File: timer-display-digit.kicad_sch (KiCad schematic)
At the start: 6 parts, among them U1 SN74LS08, U2 SN74HC595DT, U3 SN74LS08

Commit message: production ready
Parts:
- U1, U3: DigiKey# (none) -> 296-14879-1-ND
- U2: DigiKey# (none) -> 296-31823-1-ND
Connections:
- net +5V: no longer U1.14 (VCC), U3.14 (VCC)
- net A: now also U1.3; no longer U1.8
- net Araw: now also U1.1; no longer U1.9
- net B: now also U1.3; no longer U1.11
- net Braw: now also U1.1; no longer U1.12
- net C: now also U3.3; no longer U3.8
- net Craw: now also U3.1; no longer U3.9
- net E: now also U3.3; no longer U3.6
- net Eraw: now also U3.1; no longer U3.4
- net F: now also U1.3; no longer U1.6
- net Fraw: now also U1.1; no longer U1.4
- net GND: now also U3.1, U3.2; no longer U1.7 (GND), U3.12, U3.13, U3.7 (GND)
- net PWM: now also U1.2, U1.2, U1.2, U3.2, U3.2; no longer U1.10, U1.13, U1.5, U3.10, U3.5

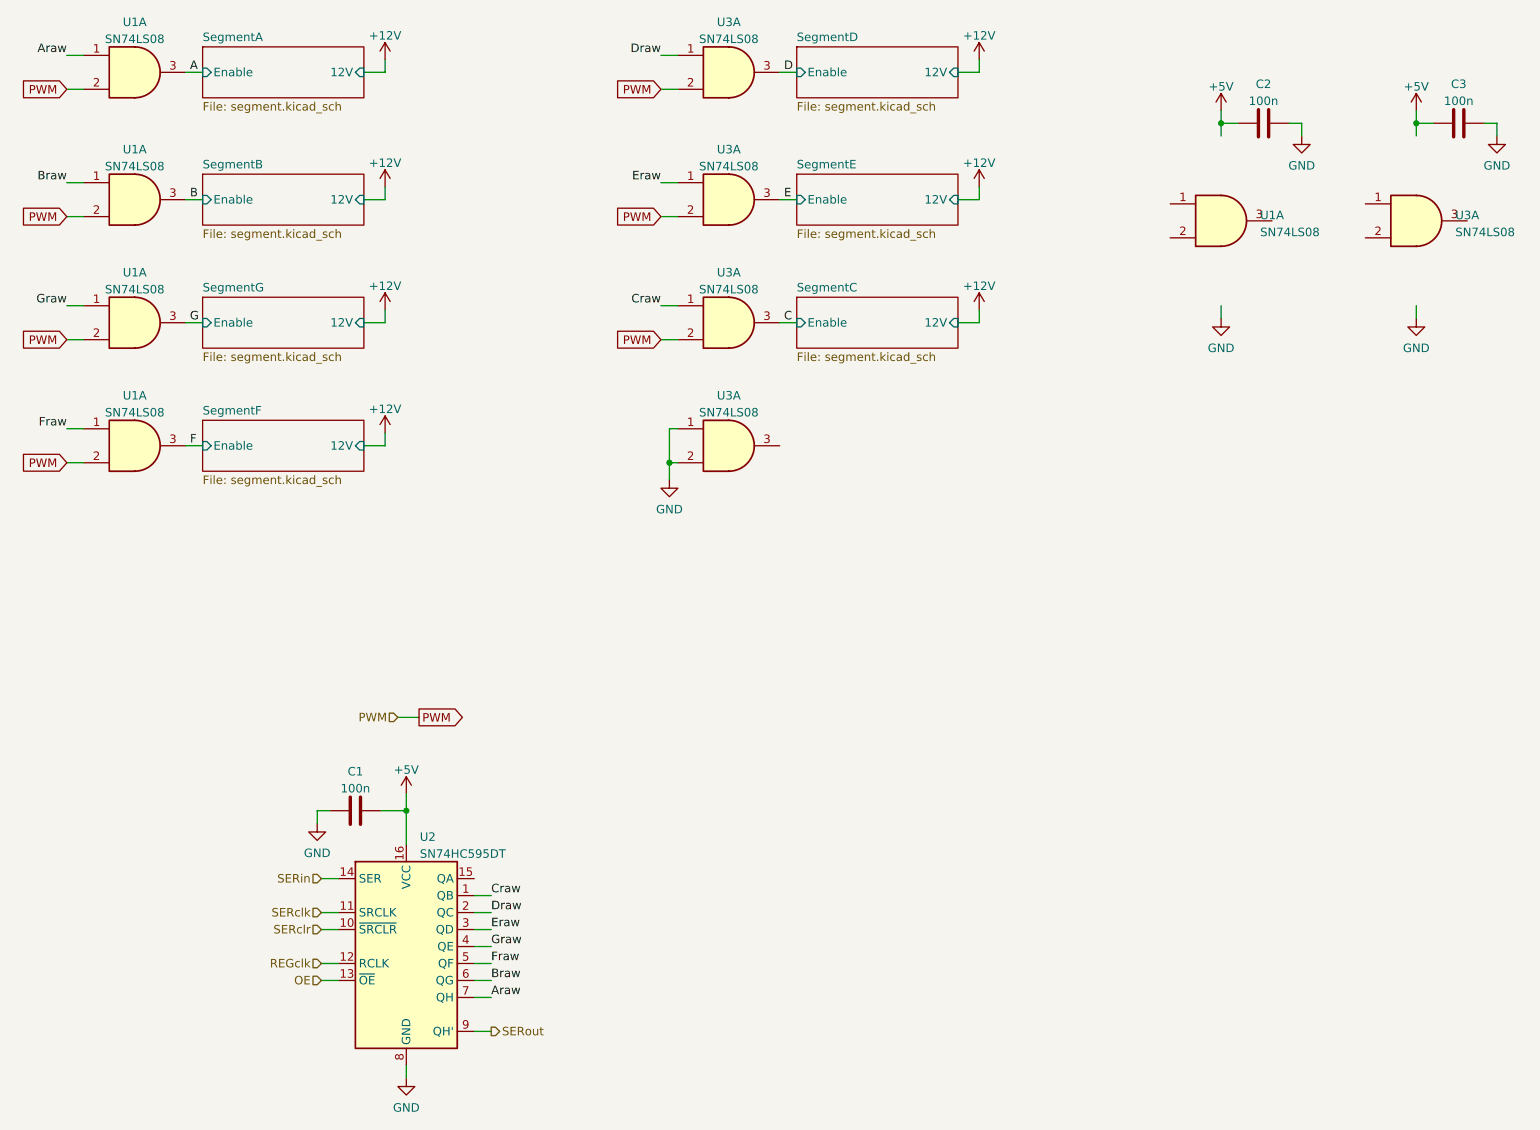
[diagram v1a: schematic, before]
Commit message: 7.0.1 -> 7.0.10
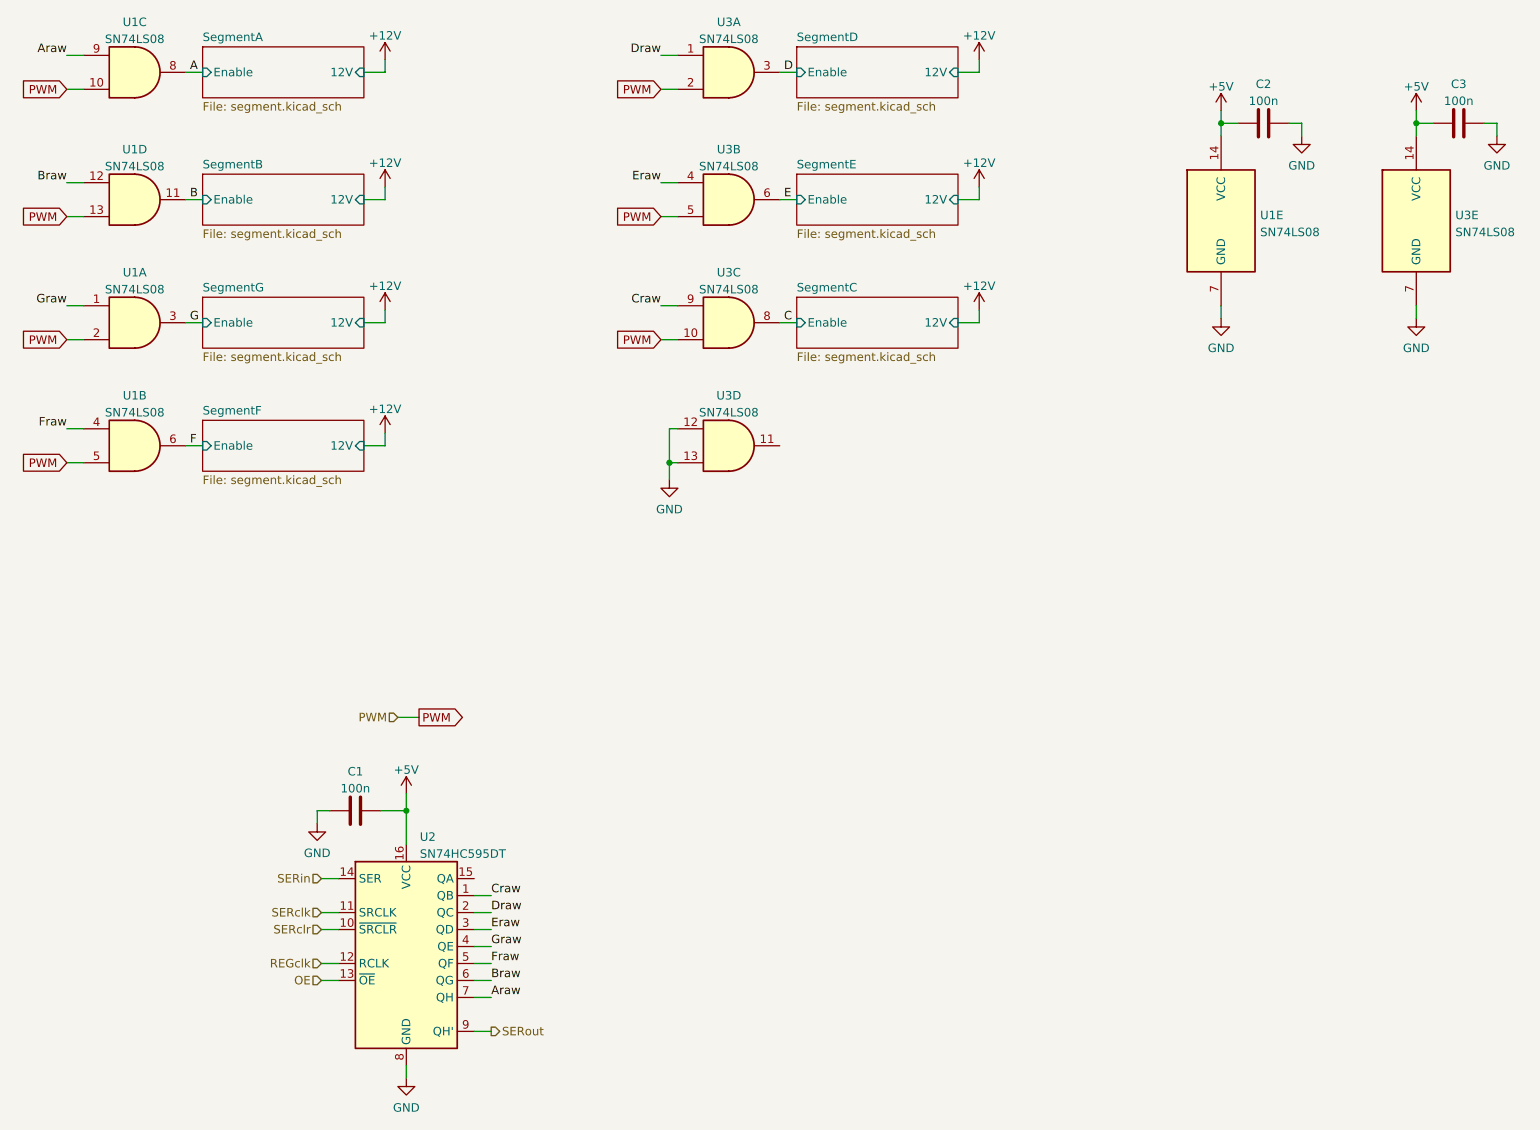
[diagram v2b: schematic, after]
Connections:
- net +5V: now also U1.14 (VCC), U3.14 (VCC)
- net A: now also U1.8; no longer U1.3
- net Araw: now also U1.9; no longer U1.1
- net B: now also U1.11; no longer U1.3
- net Braw: now also U1.12; no longer U1.1
- net C: now also U3.8; no longer U3.3
- net Craw: now also U3.9; no longer U3.1
- net E: now also U3.6; no longer U3.3
- net Eraw: now also U3.4; no longer U3.1
- net F: now also U1.6; no longer U1.3
- net Fraw: now also U1.4; no longer U1.1
- net GND: now also U1.7 (GND), U3.12, U3.13, U3.7 (GND); no longer U3.1, U3.2
- net PWM: now also U1.10, U1.13, U1.5, U3.10, U3.5; no longer U1.2, U1.2, U1.2, U3.2, U3.2
